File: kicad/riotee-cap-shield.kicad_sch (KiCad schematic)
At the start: 11 parts, among them J1 Conn_01x12, J2 Conn_01x10, SW1 SW_DIP_x08

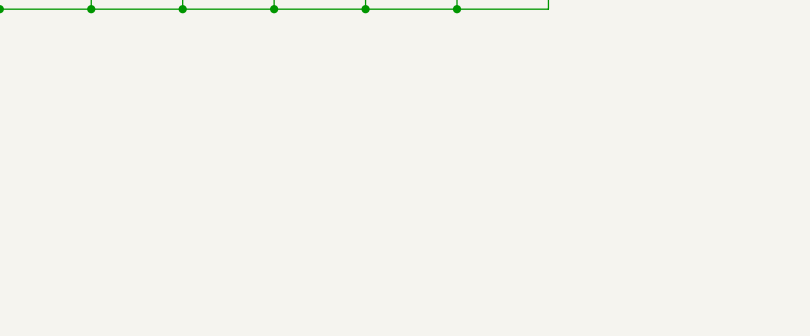
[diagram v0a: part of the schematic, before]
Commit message: add MPNs in schematics
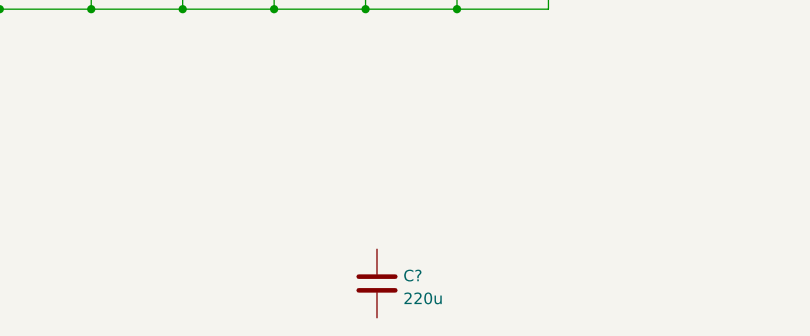
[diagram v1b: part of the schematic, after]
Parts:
- added C?: 220u, Capacitor_SMD:C_1210_3225Metric, symbol Device:C
- C1, C2, C3: MPN (none) -> GRM21BR61A476ME15K
- C4, C5, C6: MPN (none) -> GRM31CR60J227ME11K
- C7: MPN (none) -> FG0H103ZF
- C8: MPN (none) -> FGH0H224ZF
- J1: MPN (none) -> PRT-14322
- J2: MPN (none) -> PRT-11376
- SW1: MPN (none) -> 1-1825058-9
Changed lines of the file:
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@@
+      (effects (font (size 1.27 1.27)) hide)
+    )
+    (property "MPN" "GRM21BR61A476ME15K" (id 4) (at 93.98 87.63 0)
       (effects (font (size 1.27 1.27)) hide)
     )
@@
       (effects (font (size 1.27 1.27)) hide)
     )
+    (property "MPN" "FG0H103ZF" (id 4) (at 144.78 87.63 0)
+      (effects (font (size 1.27 1.27)) hide)
+    )
     (pin "1")
     (pin "2")
@@
     )
     (property "Datasheet" "~" (id 3) (at 104.14 87.63 0)
+      (effects (font (size 1.27 1.27)) hide)
+    )
+    (property "MPN" "GRM21BR61A476ME15K" (id 4) (at 104.14 87.63 0)
       (effects (font (size 1.27 1.27)) hide)
     )
@@
     (pin "1")
   )
+  (symbol (lib_id "Device:C") (at 135.89 123.19 0) (unit 1)
+    (in_bom yes) (on_board yes) (fields_autoplaced)
+    (property "Reference" "C?" (id 0) (at 138.811 122.3553 0)
+      (effects (font (size 1.27 1.27)) (justify left))
+    )
+    (property "Value" "220u" (id 1) (at 138.811 124.8922 0)
+      (effects (font (size 1.27 1.27)) (justify left))
+    )
+    (property "Footprint" "Capacitor_SMD:C_1210_3225Metric" (id 2) (at 136.8552 127 0)
+      (effects (font (size 1.27 1.27)) hide)
+    )
+    (property "Datasheet" "~" (id 3) (at 135.89 123.19 0)
+      (effects (font (size 1.27 1.27)) hide)
+    )
+    (property "MPN" "GRM31CR60J227ME11K" (id 4) (at 135.89 123.19 0)
+      (effects (font (size 1.27 1.27)) hide)
+    )
+    (pin "1")
+    (pin "2")
+  )
   (symbol (lib_id "Connector_Generic:Conn_01x10") (at 247.65 105.41 0) (unit 1)
     (in_bom yes) (on_board yes) (fields_autoplaced)
@@
     )
     (property "Datasheet" "~" (id 3) (at 247.65 105.41 0)
+      (effects (font (size 1.27 1.27)) hide)
+    )
+    (property "MPN" "PRT-11376" (id 4) (at 247.65 105.41 0)
       (effects (font (size 1.27 1.27)) hide)
     )
@@
       (effects (font (size 1.27 1.27)) hide)
     )
+    (property "MPN" "FGH0H224ZF" (id 4) (at 154.94 87.63 0)
+      (effects (font (size 1.27 1.27)) hide)
+    )
     (pin "1")
     (pin "2")
@@
     )
     (property "Datasheet" "~" (id 3) (at 247.65 67.31 0)
+      (effects (font (size 1.27 1.27)) hide)
+    )
+    (property "MPN" "PRT-14322" (id 4) (at 247.65 67.31 0)
       (effects (font (size 1.27 1.27)) hide)
     )
@@
       (effects (font (size 1.27 1.27)) hide)
     )
+    (property "MPN" "GRM31CR60J227ME11K" (id 4) (at 124.46 87.63 0)
+      (effects (font (size 1.27 1.27)) hide)
+    )
     (pin "1")
     (pin "2")
@@
       (effects (font (size 1.27 1.27)) hide)
     )
+    (property "MPN" "GRM21BR61A476ME15K" (id 4) (at 83.82 87.63 0)
+      (effects (font (size 1.27 1.27)) hide)
+    )
     (pin "1")
     (pin "2")
@@
       (effects (font (size 1.27 1.27)) hide)
     )
+    (property "MPN" "GRM31CR60J227ME11K" (id 4) (at 134.62 87.63 0)
+      (effects (font (size 1.27 1.27)) hide)
+    )
     (pin "1")
     (pin "2")
@@
     )
     (property "Datasheet" "~" (id 3) (at 114.3 87.63 0)
+      (effects (font (size 1.27 1.27)) hide)
+    )
+    (property "MPN" "GRM31CR60J227ME11K" (id 4) (at 114.3 87.63 0)
       (effects (font (size 1.27 1.27)) hide)
     )
@@
     )
     (property "Datasheet" "~" (id 3) (at 172.72 72.39 0)
+      (effects (font (size 1.27 1.27)) hide)
+    )
+    (property "MPN" "1-1825058-9" (id 4) (at 172.72 72.39 0)
       (effects (font (size 1.27 1.27)) hide)
     )
@@
       (reference "C8") (unit 1) (value "220m") (footprint "riotee:KM_FG0H103ZF")
     )
+    (path "/300df69c-762f-456d-be14-0bab21976866"
+      (reference "C?") (unit 1) (value "220u") (footprint "Capacitor_SMD:C_1210_3225Metric")
+    )
     (path "/8cd77b36-58e3-4bbf-a33d-5f41d0026d26"

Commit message: add conformity marks and refine BOM
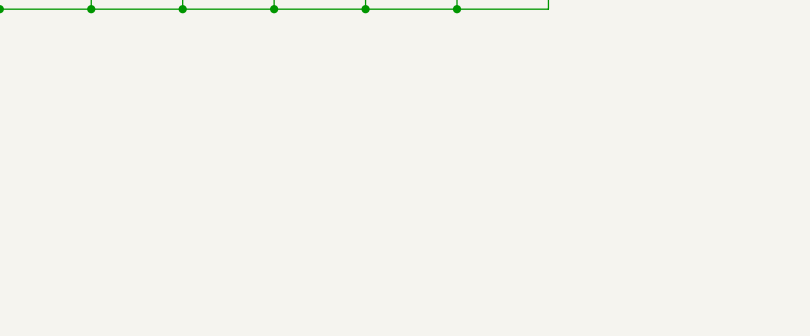
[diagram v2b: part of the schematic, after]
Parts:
- removed C?: 220u, Capacitor_SMD:C_1210_3225Metric, symbol Device:C
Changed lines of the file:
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@@
     (pin "1")
-  )
-  (symbol (lib_id "Device:C") (at 135.89 123.19 0) (unit 1)
-    (in_bom yes) (on_board yes) (fields_autoplaced)
-    (property "Reference" "C?" (id 0) (at 138.811 122.3553 0)
-      (effects (font (size 1.27 1.27)) (justify left))
-    )
-    (property "Value" "220u" (id 1) (at 138.811 124.8922 0)
-      (effects (font (size 1.27 1.27)) (justify left))
-    )
-    (property "Footprint" "Capacitor_SMD:C_1210_3225Metric" (id 2) (at 136.8552 127 0)
-      (effects (font (size 1.27 1.27)) hide)
-    )
-    (property "Datasheet" "~" (id 3) (at 135.89 123.19 0)
-      (effects (font (size 1.27 1.27)) hide)
-    )
-    (property "MPN" "GRM31CR60J227ME11K" (id 4) (at 135.89 123.19 0)
-      (effects (font (size 1.27 1.27)) hide)
-    )
-    (pin "1")
-    (pin "2")
   )
   (symbol (lib_id "Connector_Generic:Conn_01x10") (at 247.65 105.41 0) (unit 1)
@@
       (reference "C8") (unit 1) (value "220m") (footprint "riotee:KM_FG0H103ZF")
     )
-    (path "/300df69c-762f-456d-be14-0bab21976866"
-      (reference "C?") (unit 1) (value "220u") (footprint "Capacitor_SMD:C_1210_3225Metric")
-    )
     (path "/8cd77b36-58e3-4bbf-a33d-5f41d0026d26"

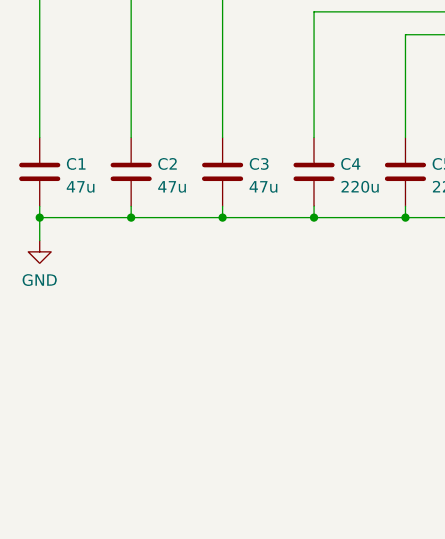
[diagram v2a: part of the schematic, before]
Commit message: migrate project to kicad 7
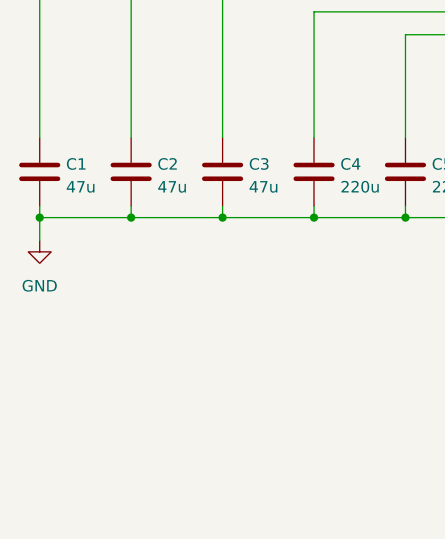
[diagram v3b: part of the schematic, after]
